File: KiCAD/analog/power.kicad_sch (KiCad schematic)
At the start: 29 parts, among them J33 Screw_Terminal_01x02, J5 Screw_Terminal_01x02, K6 Relay_SPST-NO, U13 MCP1700x-330xxTO, U6 LM2940CT-5.0, U7 LT1054, U8 LM2940CT-12, U9 LT1054

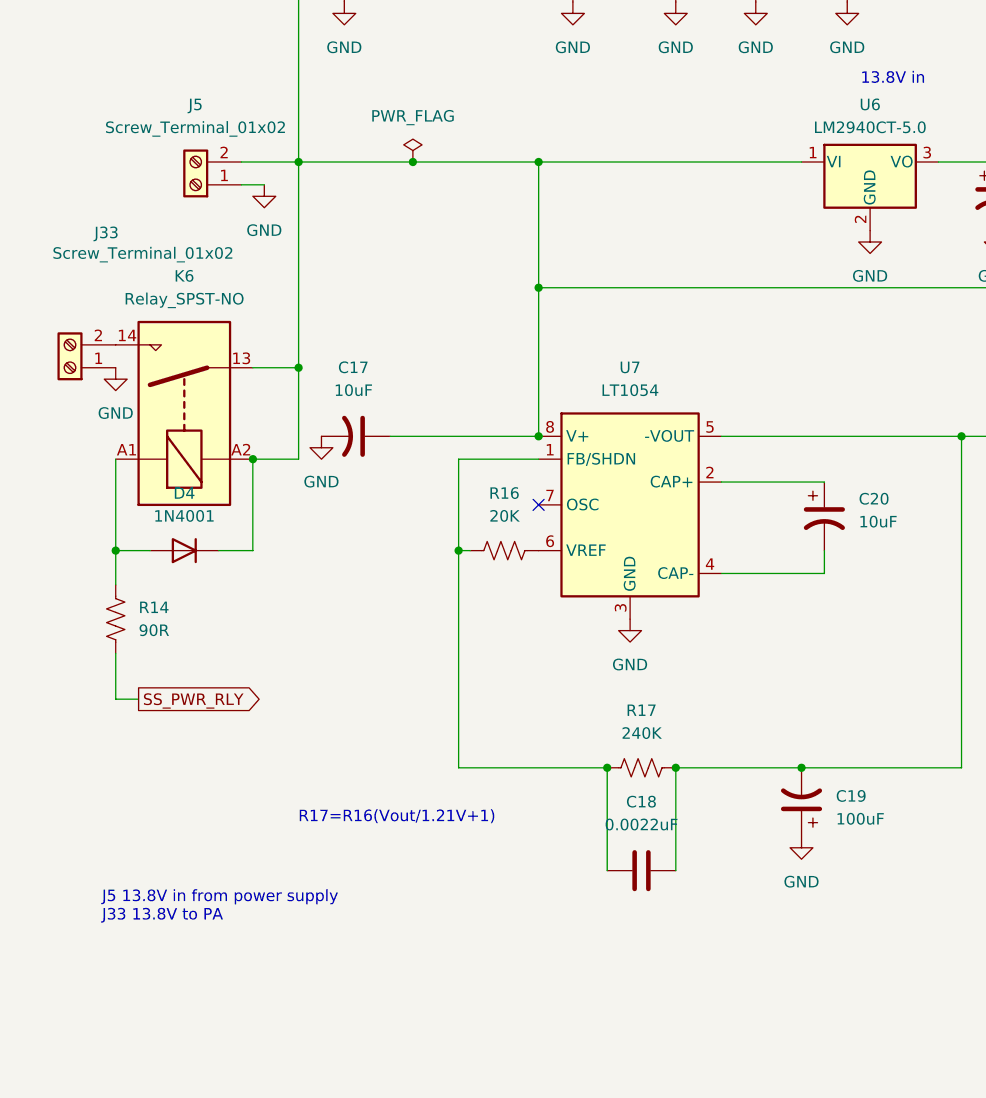
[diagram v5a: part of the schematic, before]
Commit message: KiCad revC: analog power — swap heartbeat relay to G6RL SPDT + add fault LED
K6 (RLP20 SPST-NO) replaced by K5 (Omron G6RL-1-DC12 SPDT). SPDT lets
us drive both the ss_pa power path (NO contact) and a heartbeat-fault
indicator LED (NC contact) from the same relay.

Wiring:
- Pin 4 (COM) tied to +13.8V bus
- Pin 3 (NO) -> J33 pin 2 -> cable -> ss_pa board (same as before)
- Pin 2 (NC) -> R7 (750R current limit) -> J34 pin 2 -> external LED
  -> J34 pin 1 -> GND
- Pin 1 (coil+) tied to +13.8V bus
- Pin 5 (coil-) -> R15 (90R drop) -> Q5 drain (series safety cascade
  with Q7 to GND, same Q5+Q7 chain as before)
- D5 (1N4001) flyback diode: cathode on +13.8V, anode on coil-

Behavior:
- Heartbeat alive + firmware ON: K5 energized -> COM-NO closed ->
  J33 powered -> ss_pa runs. LED OFF.
- Heartbeat fails OR firmware disable: K5 de-energized -> COM-NC
  closed -> J33 disconnected -> ss_pa cut off. LED ON (external
  panel-mount indicator shows fault to operator).

Values verified: coil ~18 mA at 12.1V effective (datasheet spec),
LED ~15.6 mA at 2V Vf, contact rating 3x headroom over 1.5A SS PA
load. See K5 trace analysis in session chat log.

Co-Authored-By: Claude Opus 4.7 <noreply@anthropic.com>
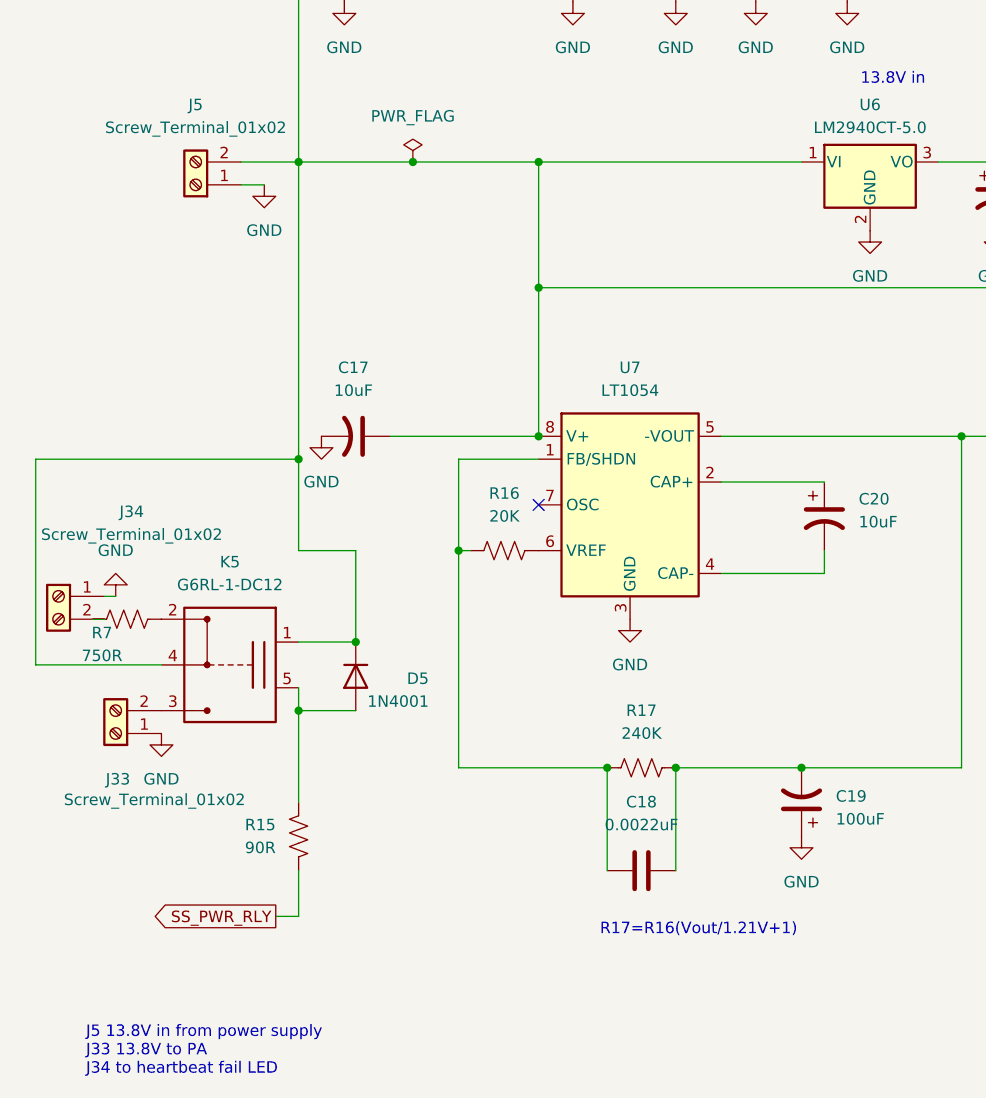
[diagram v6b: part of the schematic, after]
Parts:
- removed D4: 1N4001, Diode_THT:D_DO-41_SOD81_P10.16mm_Horizontal, symbol Diode:1N4001
- removed K6: Relay_SPST-NO, symbol Relay:Relay_SPST-NO
- removed R14: 90R, symbol Device:R_US
- added D5: 1N4001, Diode_THT:D_DO-41_SOD81_P10.16mm_Horizontal, symbol Diode:1N4001
- added J34: Screw_Terminal_01x02, symbol Connector:Screw_Terminal_01x02
- added K5: G6RL-1-DC12, xmitter:Relay_SPDT_Omron_G6RL-1, symbol xmitter:Relay_SPDT_G6RL
- added R15: 90R, symbol Device:R_US
- added R7: 750R, symbol Device:R_US
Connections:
- net GND: now also J34.1 (Pin_1)
- net SS_PWR_RLY: now also R15.2
- net at C108.1, C109.1, C15.1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: now also D5.1 (K), K5.1 (coil+), K5.4 (COM)
- net at J33.2 (Pin_2): now also K5.3 (NO)
- new net: D5.2 (A), K5.5 (coil-), R15.1
- new net: J34.2 (Pin_2), R7.1
- new net: K5.2 (NC), R7.2
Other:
- note added: "J5 13.8V in from power supply J33 13.8V to PA J34 to heartbeat fail LED"
- note removed: "J5 13.8V in from power supply J33 13.8V to PA"
- moved on the sheet: J33

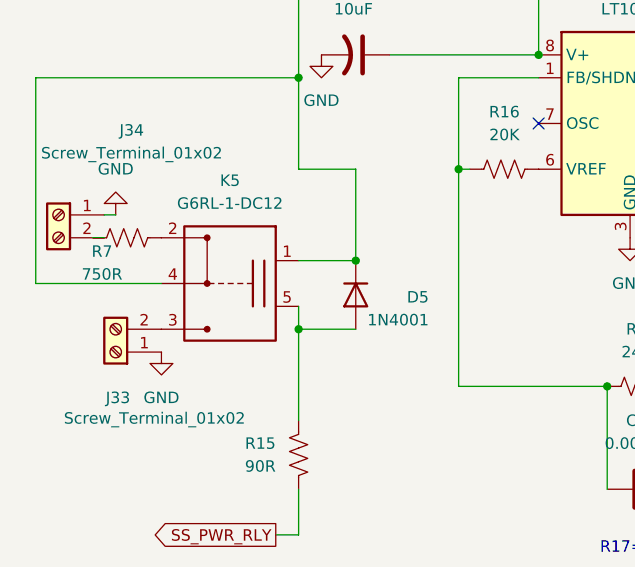
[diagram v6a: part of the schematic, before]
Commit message: revC: accumulated schematic/netlist updates + BOM tooling
- analog + ss_pa netlists regenerated to current schematic state
- interface/arduino/dac/power sheet updates on analog
- fault_shutdown and pa_stage edits on ss_pa (footprint assignments)
- assign_cap_footprints.py: additional VALUE_TO_FOOTPRINT entries
- gen_board_boms.py: per-board BOM generator (multi-sheet .xlsx by
  component category, first-match-wins bucketing, DNP exclusion)
- gen_total_bom.py: consolidated BOM across analog + frontpanel + ss_pa
  for a single Mouser order, board-prefixed references, mixed-footprint
  flagging per Value row

Co-Authored-By: Claude Opus 4.7 <noreply@anthropic.com>
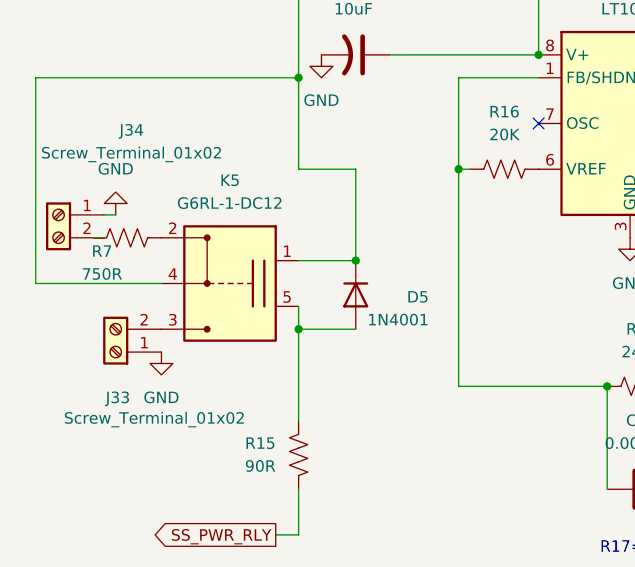
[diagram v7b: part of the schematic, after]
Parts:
- C11, C13, C17, C20: footprint (none) -> Capacitor_THT:CP_Radial_D5.0mm_P2.00mm
- C12, C18: footprint (none) -> Capacitor_THT:C_Disc_D5.0mm_W2.5mm_P5.00mm
- C14, C19: footprint (none) -> Capacitor_THT:CP_Radial_D8.0mm_P5.00mm
- C15: footprint (none) -> Capacitor_THT:C_Rect_L7.2mm_W4.5mm_P5.00mm
- J33, J34, J5: footprint (none) -> TerminalBlock_Phoenix:TerminalBlock_Phoenix_MKDS-1,5-2_1x02_P5.00mm_Horizontal
- R15, R16, R17, R7: footprint (none) -> Resistor_THT:R_Axial_DIN0207_L6.3mm_D2.5mm_P10.16mm_Horizontal
- U7, U9: footprint (none) -> Package_DIP:DIP-8_W7.62mm
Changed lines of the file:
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@@
 			)
 		)
-		(property "Footprint" ""
+		(property "Footprint" "Capacitor_THT:CP_Radial_D8.0mm_P5.00mm"
 			(at 247.65 59.69 0)
 			(hide yes)
@@
 			)
 		)
-		(property "Footprint" ""
+		(property "Footprint" "Capacitor_THT:C_Rect_L7.2mm_W4.5mm_P5.00mm"
 			(at 191.4652 86.36 0)
 			(hide yes)
@@
 			)
 		)
-		(property "Footprint" ""
+		(property "Footprint" "Capacitor_THT:CP_Radial_D5.0mm_P2.00mm"
 			(at 49.53 91.44 0)
 			(hide yes)
@@
 			)
 		)
-		(property "Footprint" ""
+		(property "Footprint" "Package_DIP:DIP-8_W7.62mm"
 			(at 82.55 101.6 0)
 			(hide yes)
@@
 			)
 		)
-		(property "Footprint" ""
+		(property "Footprint" "Capacitor_THT:CP_Radial_D8.0mm_P5.00mm"
 			(at 99.06 132.08 0)
 			(hide yes)
@@
 			)
 		)
-		(property "Footprint" ""
+		(property "Footprint" "Resistor_THT:R_Axial_DIN0207_L6.3mm_D2.5mm_P10.16mm_Horizontal"
 			(at 81.534 127.254 90)
 			(hide yes)
@@
 			)
 		)
-		(property "Footprint" ""
+		(property "Footprint" "Resistor_THT:R_Axial_DIN0207_L6.3mm_D2.5mm_P10.16mm_Horizontal"
 			(at 42.164 136.144 90)
 			(hide yes)
@@
 			)
 		)
-		(property "Footprint" ""
+		(property "Footprint" "TerminalBlock_Phoenix:TerminalBlock_Phoenix_MKDS-1,5-2_1x02_P5.00mm_Horizontal"
 			(at 16.51 109.22 0)
 			(hide yes)
@@
 			)
 		)
-		(property "Footprint" ""
+		(property "Footprint" "Capacitor_THT:CP_Radial_D5.0mm_P2.00mm"
 			(at 226.06 59.69 0)
 			(hide yes)
@@
 			)
 		)
-		(property "Footprint" ""
+		(property "Footprint" "TerminalBlock_Phoenix:TerminalBlock_Phoenix_MKDS-1,5-2_1x02_P5.00mm_Horizontal"
 			(at 22.86 124.46 0)
 			(hide yes)
@@
 			)
 		)
-		(property "Footprint" ""
+		(property "Footprint" "Capacitor_THT:CP_Radial_D5.0mm_P2.00mm"
 			(at 120.65 64.77 0)
 			(hide yes)
@@
 			)
 		)
-		(property "Footprint" ""
+		(property "Footprint" "Package_DIP:DIP-8_W7.62mm"
 			(at 208.28 85.09 0)
 			(hide yes)
@@
 			)
 		)
-		(property "Footprint" ""
+		(property "Footprint" "Resistor_THT:R_Axial_DIN0207_L6.3mm_D2.5mm_P10.16mm_Horizontal"
 			(at 66.294 103.124 90)
 			(hide yes)
@@
 			)
 		)
-		(property "Footprint" ""
+		(property "Footprint" "Resistor_THT:R_Axial_DIN0207_L6.3mm_D2.5mm_P10.16mm_Horizontal"
 			(at 24.384 110.744 90)
 			(hide yes)
@@
 			)
 		)
-		(property "Footprint" ""
+		(property "Footprint" "Capacitor_THT:C_Disc_D5.0mm_W2.5mm_P5.00mm"
 			(at 133.0452 68.58 0)
 			(hide yes)
@@
 			)
 		)
-		(property "Footprint" ""
+		(property "Footprint" "Capacitor_THT:CP_Radial_D5.0mm_P2.00mm"
 			(at 101.6 100.33 0)
 			(hide yes)
@@
 			)
 		)
-		(property "Footprint" ""
+		(property "Footprint" "TerminalBlock_Phoenix:TerminalBlock_Phoenix_MKDS-1,5-2_1x02_P5.00mm_Horizontal"
 			(at 31.75 63.5 0)
 			(hide yes)
@@
 			)
 		)
-		(property "Footprint" ""
+		(property "Footprint" "Capacitor_THT:C_Disc_D5.0mm_W2.5mm_P5.00mm"
 			(at 77.47 140.6652 0)
 			(hide yes)

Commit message: revD: drop stale LPF sub-sheets from analog + ss_pa, scrub 13.8V text comments
- Remove hierarchical LPF sub-sheets from analog and ss_pa roots; LPF
  now lives in its own project (KiCAD/Output LPF/).
- Delete the skeleton lpf.kicad_sch files and corresponding entries
  from both .kicad_pro sheet-UUID lists.
- Scrub two stale text annotations on analog/power.kicad_sch:
  "13.8V in" -> "Shack supply in" and the J5/J33/J34 legend box.
  13.8V now only appears on ss_pa and the shared +13.8V power-symbol
  definition in xmitter.kicad_sym.

Co-Authored-By: Claude Opus 4.7 <noreply@anthropic.com>
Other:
- note added: "J5 shack supply in J33 shack supply to PA J34 to heartbeat fail LED"
- note added: "Shack supply in"
- note removed: "13.8V in"
- note removed: "J5 13.8V in from power supply J33 13.8V to PA J34 to heartbeat fail LED"
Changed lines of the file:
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@@
 	(generator_version "10.0")
 	(paper "A4")
-	(text "13.8V in"
+	(text "Shack supply in"
 		(exclude_from_sim no)
 		(at 109.22 51.816 0)
@@
 		)
 	)
-	(text "J5 13.8V in from power supply\nJ33 13.8V to PA\nJ34 to heartbeat fail LED\n"
+	(text "J5 shack supply in\nJ33 shack supply to PA\nJ34 to heartbeat fail LED\n"
 		(exclude_from_sim no)
-		(at 19.558 159.766 0)
+		(at 16.764 85.598 0)
 		(effects
 			(font
